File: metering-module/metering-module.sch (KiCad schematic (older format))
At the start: 37 parts, among them J1 North, J2 South, J3 West, J4 East, Q1 MMBT3904, Q2 MMBT3904, U1 LTV-817S, U2 LTV-817S, U3 BA033CC0FP-E2, U4 MAX3486, U5 MAX3486, U6 MCP23008-xSO

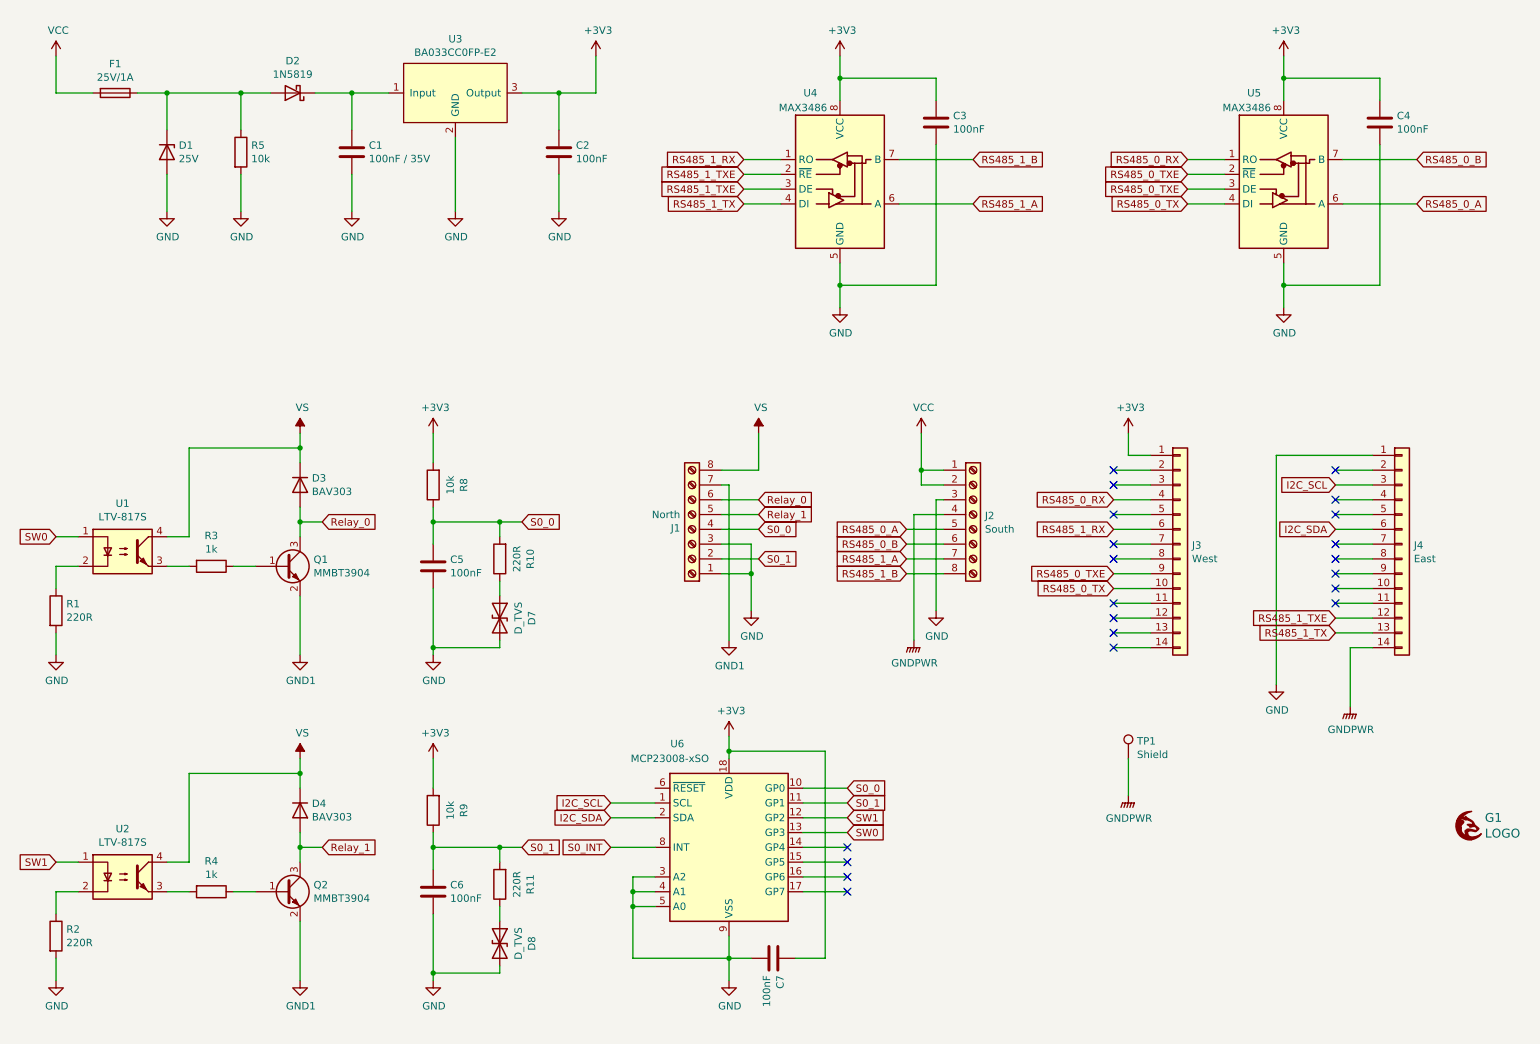
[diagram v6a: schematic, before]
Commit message: Added metering module to CI build
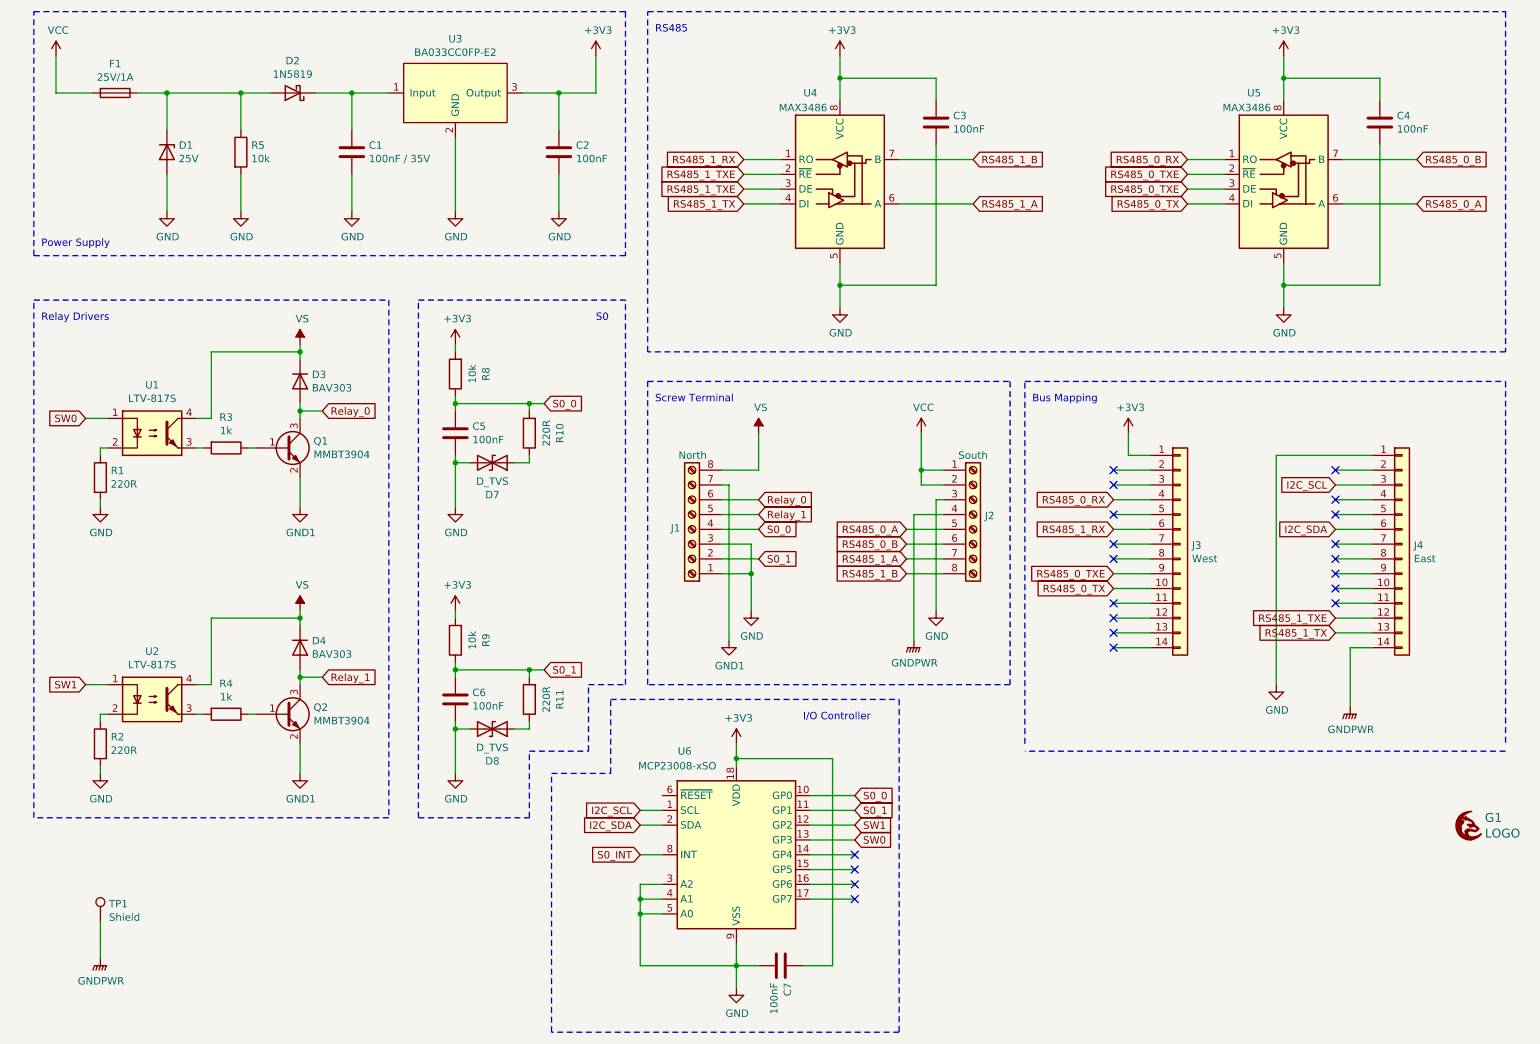
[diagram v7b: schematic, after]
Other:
- note added: "Bus Mapping"
- note added: "I/O Controller"
- note added: "Power Supply"
- note added: "RS485"
- note added: "Relay Drivers"
- note added: "S0"
- note added: "Screw Terminal"
- moved on the sheet: C5, C6, C7, D3, D4, D7, D8, Q1, Q2, R1, R10, R11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

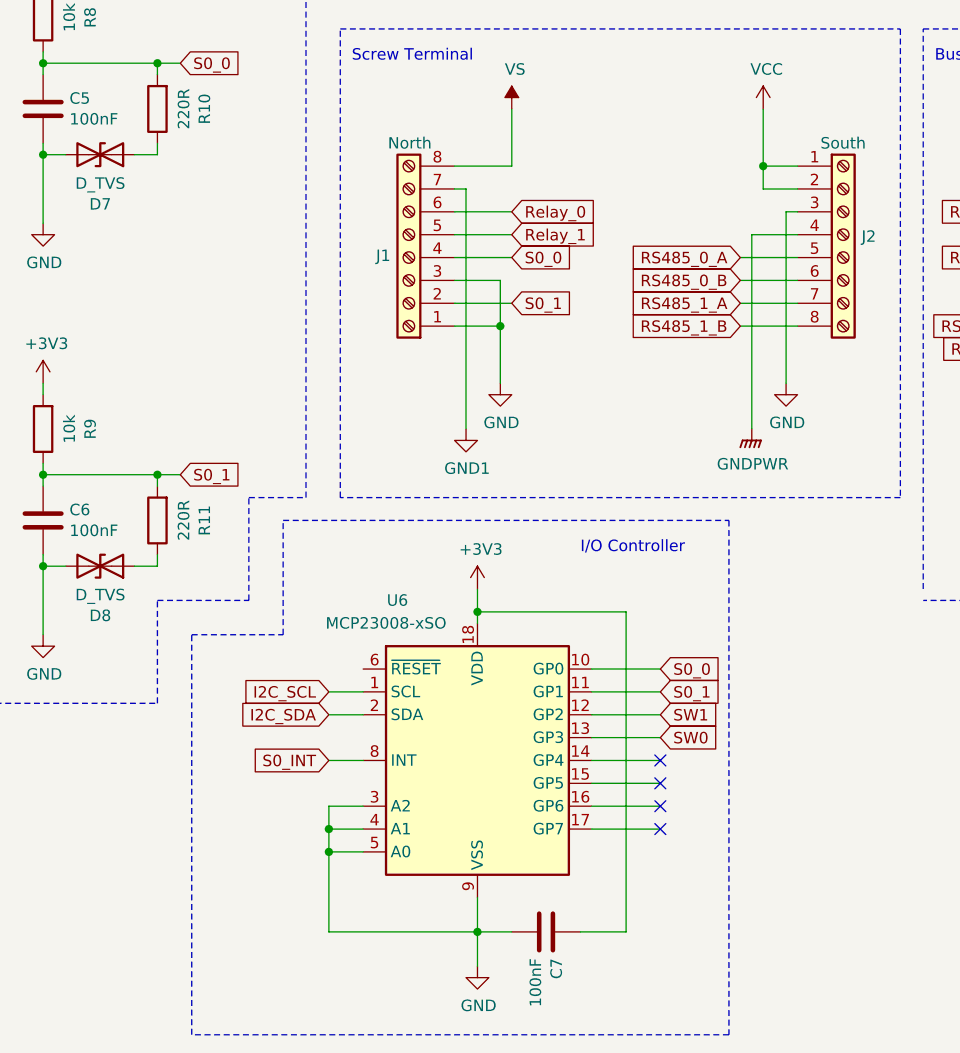
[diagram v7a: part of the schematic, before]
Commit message: Fix Footprint of MCP23009
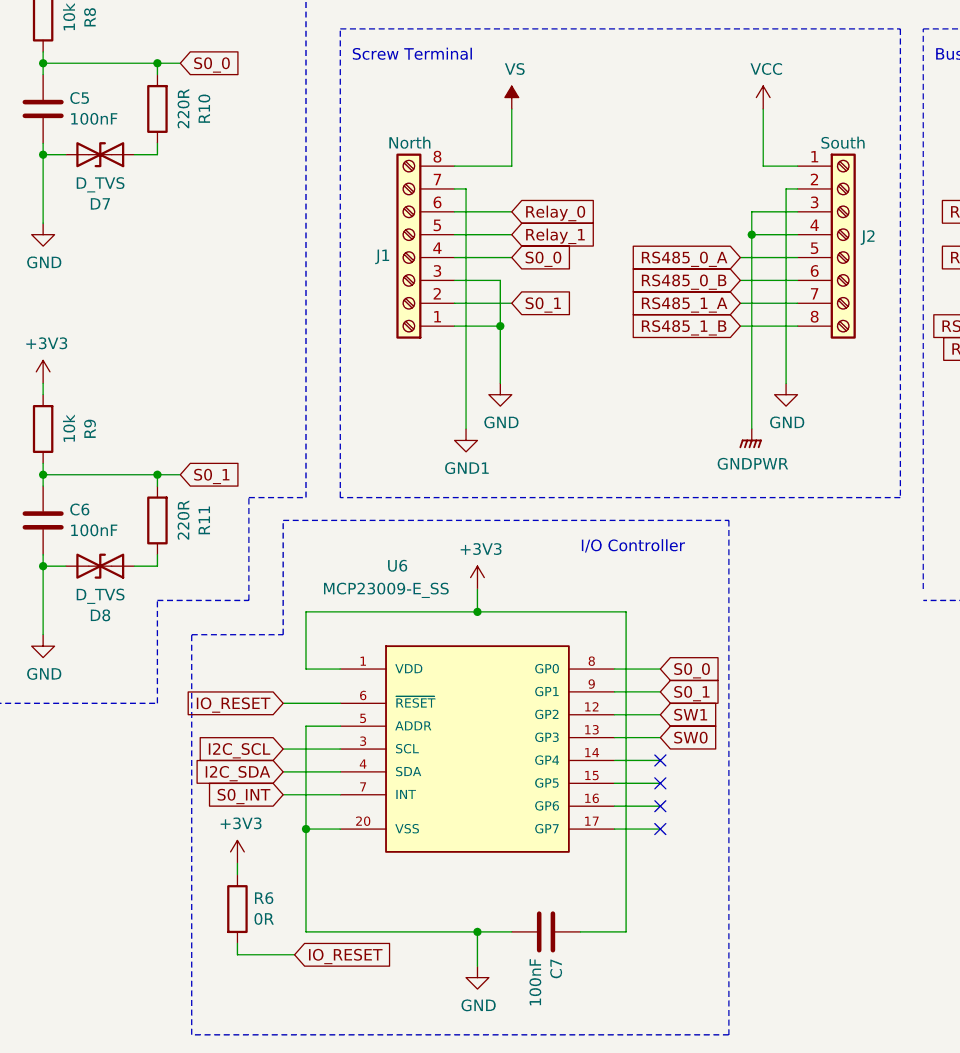
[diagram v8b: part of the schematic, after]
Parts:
- removed U6: MCP23008-xSO, Package_SO:SOIC-18W_7.5x11.6mm_P1.27mm, symbol Interface_Expansion:MCP23008-xSO
- added R6: 0R, Resistor_SMD:R_1206_3216Metric_Pad1.30x1.75mm_HandSolder, symbol Device:R
- added U6: MCP23009-E_SS, SOP65P780X200-20N, symbol MCP23009-E_SS:MCP23009-E_SS
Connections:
- net +3V3: now also R6.1, U6.1 (VDD)
- net GND: now also J2.2 (Pin_2), U6.20 (VSS), U6.5 (ADDR); no longer J2.3 (Pin_3)
- net GNDPWR: now also J2.3 (Pin_3)
- net I2C_SCL: now also U6.3 (SCL)
- net I2C_SDA: now also U6.4 (SDA)
- net S0_0: now also U6.8 (GP0)
- net S0_1: now also U6.9 (GP1)
- net S0_INT: now also U6.7 (INT)
- net SW0: now also U6.13 (GP3)
- net SW1: now also U6.12 (GP2)
- net VCC: no longer J2.2 (Pin_2)
- new net IO_RESET: R6.2, U6.6 (~RESET)
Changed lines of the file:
@@
 	8800 2100 9050 2100
-$Comp
-L Connector:Screw_Terminal_01x08 J2
-U 1 1 61A443AD
-P 7350 4200
-F 0 "J2" H 7430 4192 50  0000 L CNN
-F 1 "South" H 7250 4600 50  0000 L CNN
-F 2 "footprints:PHOENIX_1727078" H 7350 4200 50  0001 C CNN
-F 3 "https://www.mouser.de/datasheet/2/324/4/1727078-1437530.pdf" H 7350 4200 50  0001 C CNN
-F 4 "4.85" H 7350 4200 50  0001 C CNN "Price"
-F 5 "https://www.mouser.de/ProductDetail/Phoenix-Contact/1727078" H 7350 4200 50  0001 C CNN "Product"
-	1    7350 4200
-	1    0    0    -1
-$EndComp
 $Comp
 L Connector:Screw_Terminal_01x08 J1
@@
 	7000 3900 7150 3900
 Wire Wire Line
-	7000 4000 7150 4000
-Wire Wire Line
 	9800 4100 10050 4100
 Wire Wire Line
@@
 Wire Wire Line
 	8300 4200 8550 4200
-Wire Wire Line
-	7000 4000 7000 3900
-Connection ~ 7000 3900
-Wire Wire Line
-	7100 4850 7100 4100
-Wire Wire Line
-	7100 4100 7150 4100
 Wire Wire Line
 	7150 4200 6950 4200
@@
 	5750 5750 5750 5850
 Wire Wire Line
-	5750 7100 5750 7250
-Wire Wire Line
-	5900 7250 5750 7250
-Connection ~ 5750 7250
-Wire Wire Line
-	5750 7250 5750 7400
-Wire Wire Line
 	6200 7250 6400 7250
 Wire Wire Line
@@
 	6400 5850 5750 5850
 Connection ~ 5750 5850
-Wire Wire Line
-	5750 5850 5750 5900
 NoConn ~ 9800 4700
 NoConn ~ 8300 4900
 NoConn ~ 8300 5000
 NoConn ~ 8300 4200
-Wire Wire Line
-	6250 6100 6550 6100
-Wire Wire Line
-	6250 6200 6550 6200
-Wire Wire Line
-	6550 6300 6250 6300
-Wire Wire Line
-	6250 6400 6550 6400
 NoConn ~ 6550 6500
 NoConn ~ 6550 6600
 NoConn ~ 6550 6700
 NoConn ~ 6550 6800
-Wire Wire Line
-	6550 6600 6250 6600
-Wire Wire Line
-	6550 6700 6250 6700
-Wire Wire Line
-	6550 6800 6250 6800
-Text GLabel 5100 6300 0    50   Input ~ 0
+Text GLabel 4900 6550 0    50   Input ~ 0
 I2C_SDA
-Text GLabel 5100 6200 0    50   Input ~ 0
+Text GLabel 4900 6450 0    50   Input ~ 0
 I2C_SCL
 Text GLabel 9800 4300 0    50   Input ~ 0
@@
 Wire Wire Line
 	9800 4800 10050 4800
-Text GLabel 5100 6500 0    50   Input ~ 0
+Text GLabel 4900 6650 0    50   Input ~ 0
 S0_INT
-Wire Wire Line
-	5250 6700 5100 6700
-Wire Wire Line
-	5100 6700 5100 6800
-Wire Wire Line
-	5100 7250 5750 7250
-Wire Wire Line
-	5100 6800 5250 6800
-Connection ~ 5100 6800
-Wire Wire Line
-	5100 6800 5100 6900
-Wire Wire Line
-	5250 6900 5100 6900
-Connection ~ 5100 6900
-Wire Wire Line
-	5100 6900 5100 7250
 $Comp
 L Device:D_Zener D1
@@
 Connection ~ 3850 5650
 Wire Wire Line
-	5100 6200 5250 6200
-Wire Wire Line
-	5100 6300 5250 6300
-Wire Wire Line
 	1450 5600 1450 5550
 Wire Wire Line
@@
 Wire Notes Line
 	1000 2750 3400 2750
-Wire Wire Line
-	5100 6500 5250 6500
-Wire Wire Line
-	6550 6500 6250 6500
-$Comp
-L Interface_Expansion:MCP23008-xSO U6
-U 1 1 61EB4389
-P 5750 6500
-F 0 "U6" H 5400 7200 50  0000 C CNN
-F 1 "MCP23008-xSO" H 5350 7100 50  0000 C CNN
-F 2 "Package_SO:SOIC-18W_7.5x11.6mm_P1.27mm" H 5750 5450 50  0001 C CNN
-F 3 "https://www.mouser.de/datasheet/2/268/21919b-65915.pdf" H 7050 5300 50  0001 C CNN
-F 4 "1.10" H 5750 6500 50  0001 C CNN "Price"
-F 5 "https://www.mouser.de/ProductDetail/Microchip-Technology/MCP23008-E-SO" H 5750 6500 50  0001 C CNN "Product"
-	1    5750 6500
-	1    0    0    -1
-$EndComp
 Wire Notes Line
 	3600 6250 4350 6250
@@
 Text Notes 6200 5600 0    50   ~ 0
 I/O Controller
+$Comp
+L MCP23009-E_SS:MCP23009-E_SS U6
+U 1 1 62BF87F7
+P 5750 6450
+F 0 "U6" H 5400 7250 50  0000 C CNN
+F 1 "MCP23009-E_SS" H 5350 7150 50  0000 C CNN
+F 2 "SOP65P780X200-20N" H 5350 5900 50  0001 L BNN
+F 3 "https://www.mouser.de/datasheet/2/268/22121a-52412.pdf" H 5850 6300 50  0001 L BNN
+	1    5750 6450
+	1    0    0    -1
+$EndComp
+Wire Wire Line
+	6350 6100 6550 6100
+Wire Wire Line
+	6550 6200 6350 6200
+Wire Wire Line
+	6350 6300 6550 6300
+Wire Wire Line
+	6350 6400 6550 6400
+Wire Wire Line
+	5150 6100 5000 6100
+Wire Wire Line
+	5000 5850 5750 5850
+Wire Wire Line
+	6550 6500 6350 6500
+Wire Wire Line
+	6550 6600 6350 6600
+Wire Wire Line
+	6550 6700 6350 6700
+Wire Wire Line
+	6550 6800 6350 6800
+Wire Wire Line
+	4900 6450 5150 6450
+Wire Wire Line
+	4900 6550 5150 6550
+Wire Wire Line
+	4900 6650 5150 6650
+Wire Wire Line
+	5150 6800 5000 6800
+Wire Wire Line
+	5000 6800 5000 7250
+Wire Wire Line
+	5750 7400 5750 7250
+Connection ~ 5750 7250
+Wire Wire Line
+	5750 7250 5900 7250
+Wire Wire Line
+	5000 6800 5000 6350
+Wire Wire Line
+	5000 6350 5150 6350
+Connection ~ 5000 6800
+$Comp
+L Device:R R6
+U 1 1 62CD5A5B
+P 4700 7150
+F 0 "R6" H 4770 7196 50  0000 L CNN
+F 1 "0R" H 4770 7105 50  0000 L CNN
+F 2 "Resistor_SMD:R_1206_3216Metric_Pad1.30x1.75mm_HandSolder" V 4630 7150 50  0001 C CNN
+F 3 "https://www.mouser.de/datasheet/2/54/cr-1858361.pdf" H 4700 7150 50  0001 C CNN
+F 4 "0.08" H 4700 7150 50  0001 C CNN "Price"
+F 5 "https://www.mouser.de/ProductDetail/Bourns/CR1206-JW-103ELF" H 4700 7150 50  0001 C CNN "Product"
+	1    4700 7150
+	1    0    0    -1
+$EndComp
+Wire Wire Line
+	5000 7250 5750 7250
+Wire Wire Line
+	5000 6100 5000 5850
+Text GLabel 4900 6250 0    50   Input ~ 0
+IO_RESET
+Wire Wire Line
+	4900 6250 5150 6250
+$Comp
+L power:+3V3 #PWR0135
+U 1 1 62D387A4
+P 4700 6950
+F 0 "#PWR0135" H 4700 6800 50  0001 C CNN
+F 1 "+3V3" H 4715 7123 50  0000 C CNN
+F 2 "" H 4700 6950 50  0001 C CNN
+F 3 "" H 4700 6950 50  0001 C CNN
+	1    4700 6950
+	1    0    0    -1
+$EndComp
+Wire Wire Line
+	4700 6950 4700 7000
+Text GLabel 4950 7350 2    50   Input ~ 0
+IO_RESET
+Wire Wire Line
+	4950 7350 4700 7350
+Wire Wire Line
+	4700 7300 4700 7350
+$Comp
+L Connector:Screw_Terminal_01x08 J2
+U 1 1 61A443AD
+P 7350 4200
+F 0 "J2" H 7430 4192 50  0000 L CNN
+F 1 "South" H 7250 4600 50  0000 L CNN
+F 2 "footprints:PHOENIX_1727078" H 7350 4200 50  0001 C CNN
+F 3 "https://www.mouser.de/datasheet/2/324/4/1727078-1437530.pdf" H 7350 4200 50  0001 C CNN
+F 4 "4.85" H 7350 4200 50  0001 C CNN "Price"
+F 5 "https://www.mouser.de/ProductDetail/Phoenix-Contact/1727078" H 7350 4200 50  0001 C CNN "Product"
+	1    7350 4200
+	1    0    0    -1
+$EndComp
+Wire Wire Line
+	7100 4000 7150 4000
+Wire Wire Line
+	7100 4000 7100 4850
+Wire Wire Line
+	6950 4200 6950 4100
+Wire Wire Line
+	6950 4100 7150 4100
+Connection ~ 6950 4200
 $EndSCHEMATC
